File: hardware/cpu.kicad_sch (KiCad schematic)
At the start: 62 parts, among them Q5 MMBT3904, U1 H3, Y1 32kHz, Y3 24MHz

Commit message: Update crystal
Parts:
- C34: renamed from C127; value 15pF -> 18pF; LCSC Part # C1548 -> C106202
- C41: renamed from C128; value 15pF -> 18pF; LCSC Part # C1548 -> C106202
- Y2: renamed from Y3; LCSC Part # C37635323 -> C7294676
- renumbered C2 to C1, C13 to C10, C14 to C11, C15 to C12, C16 to C13, C17 to C14, C18 to C15, C19 to C16, C20 to C17, C21 to C18, C22 to C19, C1 to C2, C23 to C20, C24 to C21, C25 to C22, C26 to C23, C27 to C24, C28 to C25, C29 to C26, C30 to C27, C31 to C28, C32 to C29, C33 to C30, C129 to C31, C130 to C32, C34 to C33, C10 to C35, C35 to C36, C36 to C37, C37 to C38, C38 to C39, C39 to C40, C7 to C5, C8 to C6, C41 to C7, C11 to C8, C12 to C9, Q5 to Q1, R5 to R10, R64 to R11, R63 to R12, R66 to R13, R6 to R14, R67 to R2, R68 to R3, R61 to R4, R62 to R5, R2 to R6, R3 to R7, R65 to R8, R4 to R9, TP2 to TP1, TP3 to TP2, TP1 to TP3
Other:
- note removed: "FIXME: KEYADC"
- moved on the sheet: U1F

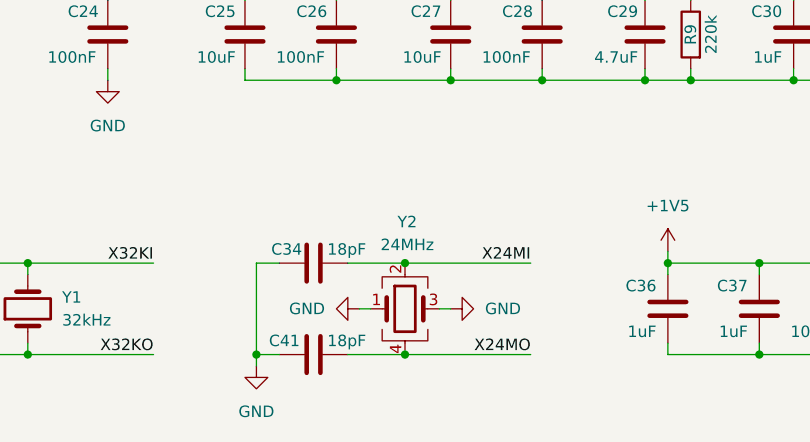
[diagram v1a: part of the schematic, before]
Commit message: Changed crystal and fix USB data lines
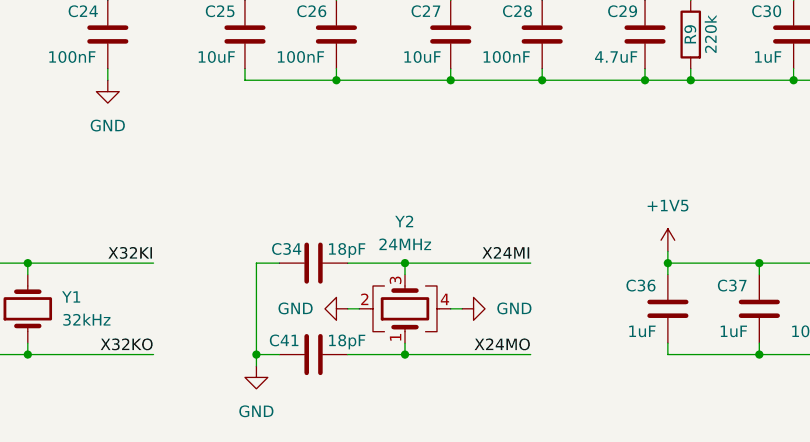
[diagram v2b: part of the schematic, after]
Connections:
- net GND: now also Y2.2, Y2.4; no longer Y2.1, Y2.3
- net X24MI: now also Y2.3; no longer Y2.2
- net X24MO: now also Y2.1; no longer Y2.4
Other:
- moved on the sheet: Y2
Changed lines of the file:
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@@
 	)
 	(junction
-		(at 86.36 246.38)
-		(diameter 0)
-		(color 0 0 0 0)
-	)
-	(junction
-		(at 86.36 256.54)
-		(diameter 0)
-		(color 0 0 0 0)
-	)
-	(junction
 		(at 78.74 226.06)
 		(diameter 0)
@@
 	)
 	(junction
+		(at 86.36 246.38)
+		(diameter 0)
+		(color 0 0 0 0)
+	)
+	(junction
 		(at 125.73 256.54)
 		(diameter 0)
@@
 	)
 	(junction
+		(at 86.36 256.54)
+		(diameter 0)
+		(color 0 0 0 0)
+	)
+	(junction
 		(at 220.98 215.9)
 		(diameter 0)
@@
 	(wire
 		(pts
+			(xy 86.36 246.38) (xy 86.36 247.65)
+		)
+		(stroke
+			(width 0)
+			(type default)
+		)
+	)
+	(wire
+		(pts
 			(xy 228.6 119.38) (xy 240.03 119.38)
 		)
@@
 	(wire
 		(pts
-			(xy 86.36 256.54) (xy 100.33 256.54)
-		)
-		(stroke
-			(width 0)
-			(type default)
-		)
-	)
-	(wire
-		(pts
 			(xy 96.52 45.72) (xy 104.14 45.72)
 		)
@@
 	(wire
 		(pts
-			(xy 90.17 251.46) (xy 91.44 251.46)
+			(xy 91.44 251.46) (xy 92.71 251.46)
 		)
 		(stroke
@@
 	(wire
 		(pts
-			(xy 82.55 251.46) (xy 81.28 251.46)
+			(xy 81.28 251.46) (xy 80.01 251.46)
 		)
 		(stroke
@@
 	(wire
 		(pts
+			(xy 86.36 256.54) (xy 100.33 256.54)
+		)
+		(stroke
+			(width 0)
+			(type default)
+		)
+	)
+	(wire
+		(pts
 			(xy 316.23 208.28) (xy 317.5 208.28)
 		)
@@
 		)
 	)
-	(wire
-		(pts
-			(xy 86.36 246.38) (xy 100.33 246.38)
-		)
-		(stroke
-			(width 0)
-			(type default)
-		)
-	)
 	(bus
 		(pts
@@
 	(wire
 		(pts
+			(xy 86.36 255.27) (xy 86.36 256.54)
+		)
+		(stroke
+			(width 0)
+			(type default)
+		)
+	)
+	(wire
+		(pts
 			(xy 125.73 186.69) (xy 125.73 187.96)
 		)
@@
 	(wire
 		(pts
+			(xy 86.36 246.38) (xy 100.33 246.38)
+		)
+		(stroke
+			(width 0)
+			(type default)
+		)
+	)
+	(wire
+		(pts
 			(xy 172.72 223.52) (xy 173.99 223.52)
 		)
@@
 	(symbol
 		(lib_id "power:GND")
-		(at 81.28 251.46 270)
+		(at 80.01 251.46 270)
 		(unit 1)
 		(exclude_from_sim no)
@@
 		(fields_autoplaced yes)
 		(property "Reference" "#PWR054"
-			(at 74.93 251.46 0)
+			(at 73.66 251.46 0)
 			(effects
 				(font
@@
 		)
 		(property "Value" "GND"
-			(at 77.47 251.4601 90)
+			(at 76.2 251.4601 90)
 			(effects
 				(font
@@
 		)
 		(property "Footprint" ""
-			(at 81.28 251.46 0)
+			(at 80.01 251.46 0)
 			(effects
 				(font
@@
 		)
 		(property "Datasheet" ""
-			(at 81.28 251.46 0)
+			(at 80.01 251.46 0)
 			(effects
 				(font
@@
 		)
 		(property "Description" "Power symbol creates a global label with name \"GND\" , ground"
-			(at 81.28 251.46 0)
+			(at 80.01 251.46 0)
 			(effects
 				(font
@@
 	(symbol
 		(lib_id "power:GND")
-		(at 91.44 251.46 90)
+		(at 92.71 251.46 90)
 		(unit 1)
 		(exclude_from_sim no)
@@
 		(fields_autoplaced yes)
 		(property "Reference" "#PWR055"
-			(at 97.79 251.46 0)
+			(at 99.06 251.46 0)
 			(effects
 				(font
@@
 		)
 		(property "Value" "GND"
-			(at 95.25 251.4599 90)
+			(at 96.52 251.4599 90)
 			(effects
 				(font
@@
 		)
 		(property "Footprint" ""
-			(at 91.44 251.46 0)
+			(at 92.71 251.46 0)
 			(effects
 				(font
@@
 		)
 		(property "Datasheet" ""
-			(at 91.44 251.46 0)
+			(at 92.71 251.46 0)
 			(effects
 				(font
@@
 		)
 		(property "Description" "Power symbol creates a global label with name \"GND\" , ground"
-			(at 91.44 251.46 0)
+			(at 92.71 251.46 0)
 			(effects
 				(font
@@
 	(symbol
 		(lib_id "Device:Crystal_GND24")
-		(at 86.36 251.46 0)
+		(at 86.36 251.46 90)
 		(unit 1)
 		(exclude_from_sim no)
@@
 		(dnp no)
 		(property "Reference" "Y2"
-			(at 86.614 241.808 0)
+			(at 86.36 241.808 90)
 			(effects
 				(font
@@
 		)
 		(property "Value" "24MHz"
-			(at 86.614 244.348 0)
+			(at 86.36 244.348 90)
 			(effects
 				(font

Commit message: Add schematic pdf
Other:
- title: Icepi CM0 -> Icepi SBC
- moved on the sheet: C7, R13, R2, R3, R5, R6, U1A
